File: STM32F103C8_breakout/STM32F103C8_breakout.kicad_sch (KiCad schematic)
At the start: 45 parts, among them J1 Conn1x1Pin-PA0_WKUP, J10 Conn1x1Pin-PA9, J11 Conn1x1Pin-PA10, J12 Conn1x1Pin-PA11, J13 Conn1x1Pin-PA12, J14 Conn1x1Pin-PA13, J15 Conn1x1Pin-PA14, J16 Conn1x1Pin-PA15, J17 Conn1x1Pin-PC13-TAMPER-RTC, J18 Conn1x1Pin-PC14-OSC32_IN, J19 Conn1x1Pin-PC15-OSC32_OUT, J2 Conn1x1Pin-PA1, J20 Conn1x1Pin-VBAT, J21 Conn1x1Pin-NRST, J22 BOOT0, J23 Conn1x1Pin-VDD, J24 Conn1x1Pin-VDDA, J25 Conn1x1Pin-PB15, J26 Conn1x1Pin-PB14, J27 Conn1x1Pin-PB13, J28 Conn1x1Pin-PB12, J29 Conn1x1Pin-PB11, J3 Conn1x1Pin-PA2, J30 Conn1x1Pin-PB10, J31 Conn1x1Pin-PB9, J32 Conn1x1Pin-PB8, J33 Conn1x1Pin-PB7, J34 Conn1x1Pin-PB6, J35 Conn1x1Pin-PB5, J36 Conn1x1Pin-PB4, J37 Conn1x1Pin-PB3, J38 Conn1x1Pin-PB2, J39 Conn1x1Pin-PB1, J4 Conn1x1Pin-PA3, J40 Conn1x1Pin-PB0, J41 Conn1x1Pin-PC0_OSC_IN, J42 Conn1x1Pin-PD1_OSC_OUT, J43 Conn1x1Pin-VSSA, J44 Conn1x1Pin-VSS, J5 Conn1x1Pin-PA4, J6 Conn1x1Pin-PA5, J7 Conn1x1Pin-PA6, J8 Conn1x1Pin-PA7, J9 Conn1x1Pin-PA8, U1 STM32F103C8T6

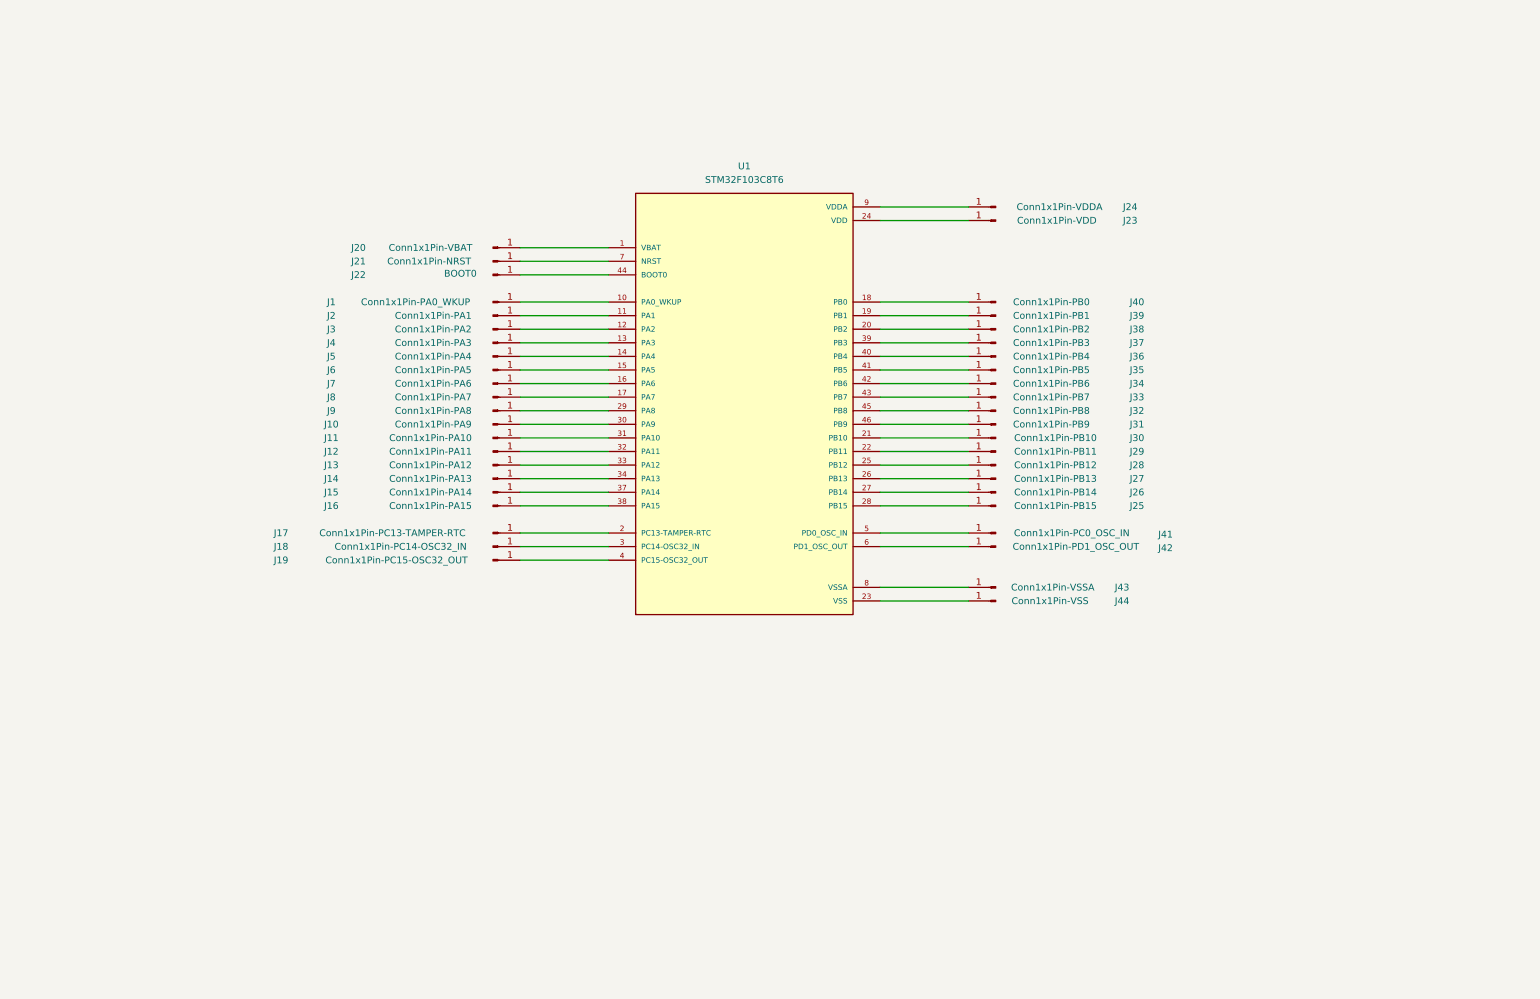
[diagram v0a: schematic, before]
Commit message: Refactored Dev. Board Schematic
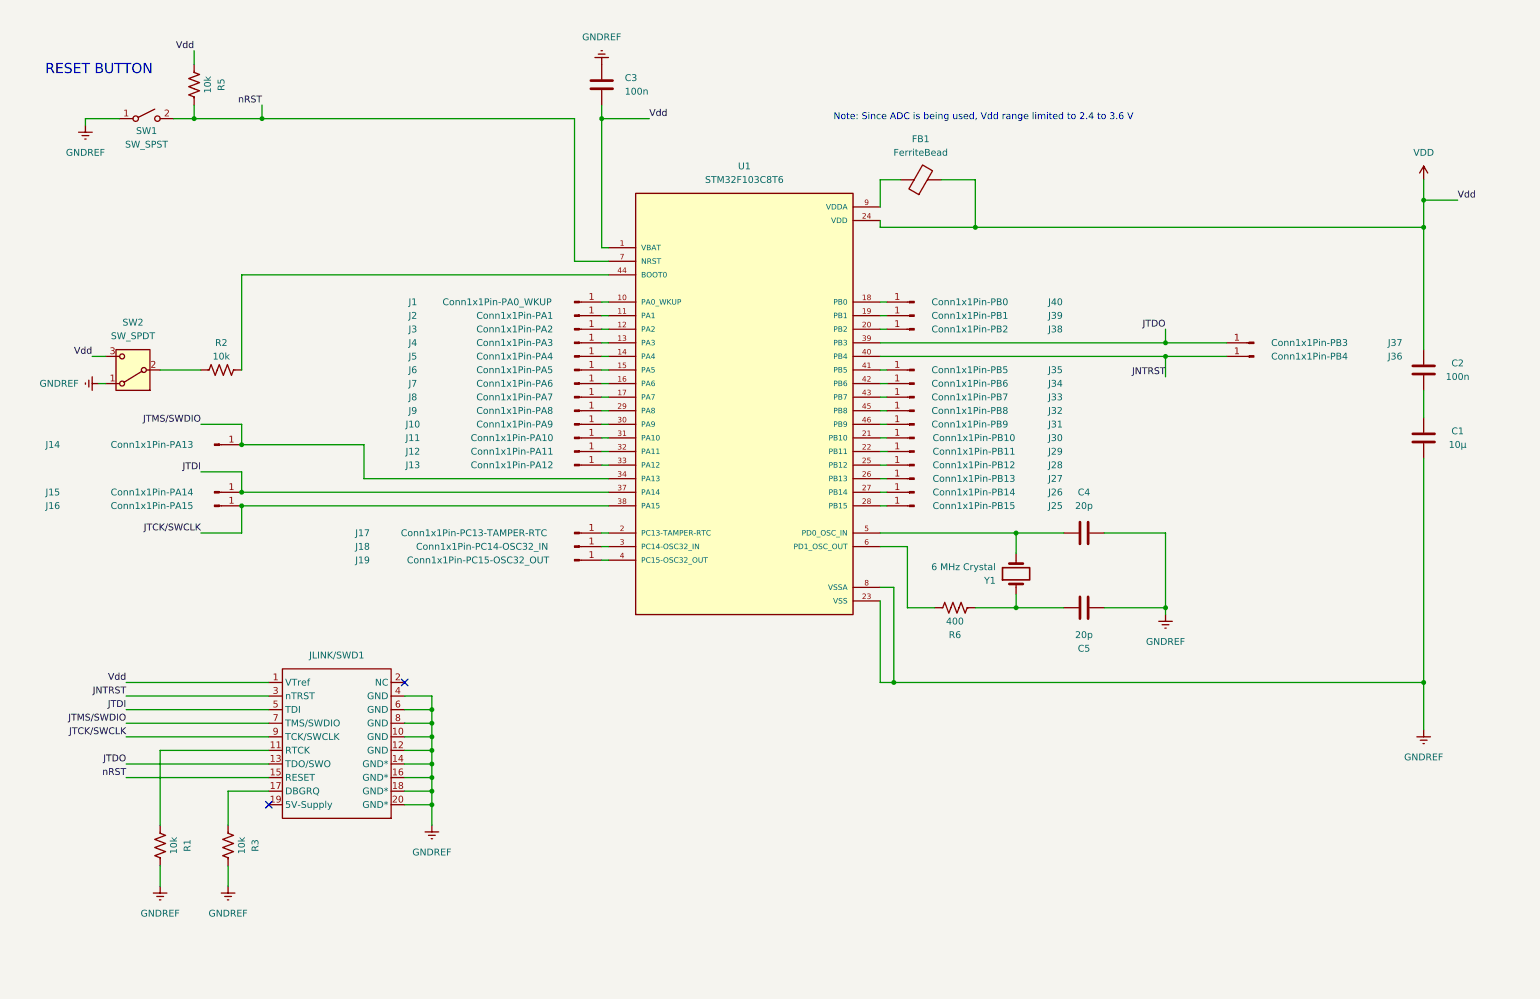
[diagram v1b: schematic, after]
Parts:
- removed J20: Conn1x1Pin-VBAT, Connector_PinHeader_2.54mm:PinHeader_1x01_P2.54mm_Horizontal, symbol Connector:Conn_01x01_Pin
- removed J21: Conn1x1Pin-NRST, Connector_PinHeader_2.54mm:PinHeader_1x01_P2.54mm_Horizontal, symbol Connector:Conn_01x01_Pin
- removed J22: BOOT0, Connector_PinHeader_2.54mm:PinHeader_1x01_P2.54mm_Horizontal, symbol Connector:Conn_01x01_Pin
- removed J23: Conn1x1Pin-VDD, Connector_PinHeader_2.54mm:PinHeader_1x01_P2.54mm_Horizontal, symbol Connector:Conn_01x01_Pin
- removed J24: Conn1x1Pin-VDDA, Connector_PinHeader_2.54mm:PinHeader_1x01_P2.54mm_Horizontal, symbol Connector:Conn_01x01_Pin
- removed J41: Conn1x1Pin-PC0_OSC_IN, Connector_PinHeader_2.54mm:PinHeader_1x01_P2.54mm_Horizontal, symbol Connector:Conn_01x01_Pin
- removed J42: Conn1x1Pin-PD1_OSC_OUT, Connector_PinHeader_2.54mm:PinHeader_1x01_P2.54mm_Horizontal, symbol Connector:Conn_01x01_Pin
- removed J43: Conn1x1Pin-VSSA, Connector_PinHeader_2.54mm:PinHeader_1x01_P2.54mm_Horizontal, symbol Connector:Conn_01x01_Pin
- removed J44: Conn1x1Pin-VSS, Connector_PinHeader_2.54mm:PinHeader_1x01_P2.54mm_Horizontal, symbol Connector:Conn_01x01_Pin
- added C1: 10μ, symbol Device:C
- added C2, C3: 100n, symbol Device:C
- added C4, C5: 20p, symbol Device:C
- added FB1: FerriteBead, symbol Device:FerriteBead
- added JLINK/SWD1: ~, symbol KnockOut_Symbols:KnockOut_Debugger
- added R1, R2, R3, R5: 10k, symbol Device:R_US
- added R6: 400, symbol Device:R_US
- added SW1: SW_SPST, symbol Switch:SW_SPST
- added SW2: SW_SPDT, symbol Switch:SW_SPDT
- added Y1: 6 MHz Crystal, symbol Device:Crystal
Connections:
- net VSS is gone; now on net GNDREF: U1.23 (VSS), U1.35 (VSS), U1.47 (VSS)
- net VDD: now also U1.1 (VBAT), C2.2, C3.1, FB1.2, JLINK/SWD1.1 (VTref), R5.1, SW2.3 (C)
- net JTDO: now reaches J37.1 (Pin_1), U1.39 (PB3)
- net JTDO: now also JLINK/SWD1.13 (TDO/SWO)
- net JTMS/SWDIO: now reaches J14.1 (Pin_1), U1.34 (PA13)
- net JTMS/SWDIO: now also JLINK/SWD1.7 (TMS/SWDIO)
- net JTDI: now reaches J15.1 (Pin_1), U1.37 (PA14)
- net JTDI: now also JLINK/SWD1.5 (TDI)
- net JTCK/SWCLK: now reaches J16.1 (Pin_1), U1.38 (PA15)
- net JTCK/SWCLK: now also JLINK/SWD1.9 (TCK/SWCLK)
- net JNTRST: now reaches J36.1 (Pin_1), U1.40 (PB4)
- net JNTRST: now also JLINK/SWD1.3 (nTRST)
- net at U1.44 (BOOT0): now also R2.2
- net at U1.5 (PD0_OSC_IN): now also C4.1, Y1.2
- net at U1.6 (PD1_OSC_OUT): now also R6.2
- net nRST: now reaches U1.7 (NRST)
- net nRST: now also JLINK/SWD1.15 (RESET), R5.2, SW1.2 (B)
- net GNDREF: now reaches U1.8 (VSSA)
- net GNDREF: now also C1.1, C3.2, C4.2, C5.1, JLINK/SWD1.10 (GND), JLINK/SWD1.12 (GND), JLINK/SWD1.14 (GND*), JLINK/SWD1.16 (GND*), JLINK/SWD1.18 (GND*), JLINK/SWD1.20 (GND*), JLINK/SWD1.4 (GND), JLINK/SWD1.6 (GND), JLINK/SWD1.8 (GND), R1.2, R3.2, SW1.1 (A), SW2.1 (A)
- net at U1.9 (VDDA): now also FB1.1
- new net: C5.2, R6.1, Y1.1
- new net: C1.2, C2.1
- new net: JLINK/SWD1.11 (RTCK), R1.1
- new net: JLINK/SWD1.17 (DBGRQ), R3.1
- new net: R2.1, SW2.2 (B)
- no-connect marks 0 -> 2
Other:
- note added: "Note: Since ADC is being used, Vdd range limited to 2.4 to 3.6 V"
- note added: "RESET BUTTON"
- moved on the sheet: J1, J10, J11, J12, J13, J14, J15, J16, J17, J18, J19, J2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

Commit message: Updated schematic to (mostly) complete Dev Board.
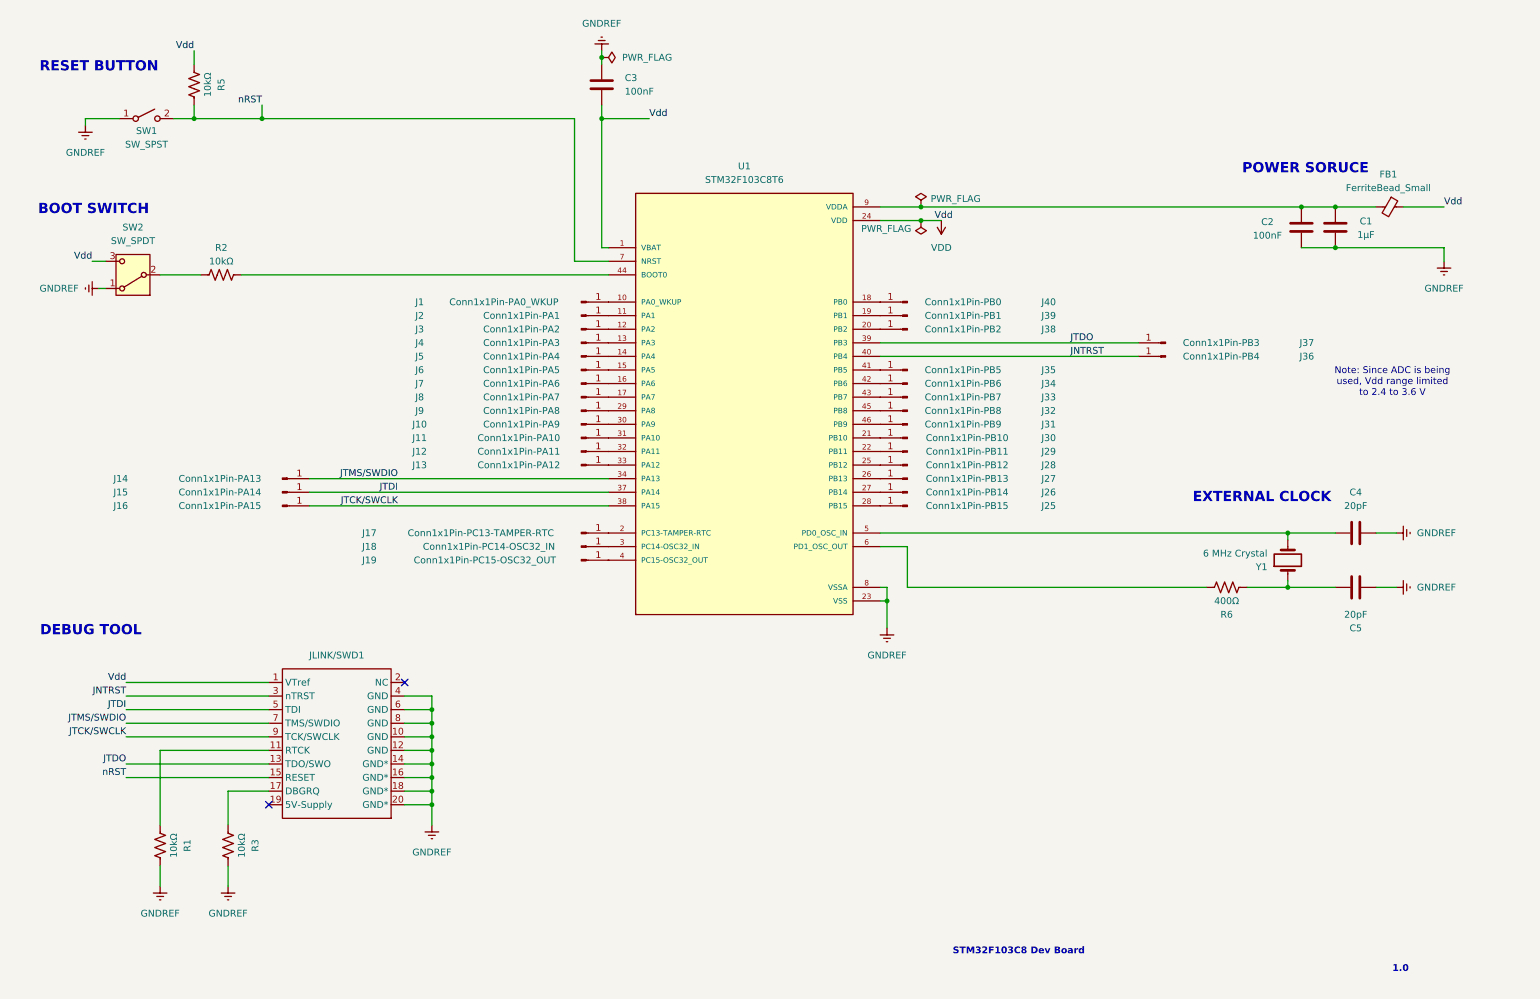
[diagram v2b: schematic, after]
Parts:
- removed FB1: FerriteBead, symbol Device:FerriteBead
- added FB1: FerriteBead_Small, Inductor_SMD:L_0805_2012Metric_Pad1.05x1.20mm_HandSolder, symbol Device:FerriteBead_Small
- C1: value 10μ -> 1μF; footprint (none) -> Capacitor_SMD:C_0805_2012Metric_Pad1.18x1.45mm_HandSolder
- C2, C3: value 100n -> 100nF; footprint (none) -> Capacitor_SMD:C_0805_2012Metric_Pad1.18x1.45mm_HandSolder
- C4, C5: value 20p -> 20pF; footprint (none) -> Capacitor_SMD:C_0805_2012Metric_Pad1.18x1.45mm_HandSolder
- JLINK/SWD1: footprint (none) -> Connector_IDC:IDC-Header_2x10_P2.54mm_Vertical
- R1, R2, R3, R5: value 10k -> 10kΩ; footprint (none) -> Resistor_SMD:R_0805_2012Metric_Pad1.20x1.40mm_HandSolder
- R6: value 400 -> 400Ω; footprint (none) -> Resistor_SMD:R_0805_2012Metric_Pad1.20x1.40mm_HandSolder
- Y1: footprint (none) -> Crystal:Crystal_SMD_HC49-SD_HandSoldering
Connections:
- net GNDREF: now also C1.2, C2.2; no longer C1.1
- net VDD: now also FB1.1; no longer C2.2
- net at U1.9 (VDDA): now also C1.1, C2.1, FB1.2
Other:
- note added: "1.0"
- note added: "BOOT SWITCH"
- note added: "DEBUG TOOL"
- note added: "EXTERNAL CLOCK"
- note added: "POWER SORUCE"
- note added: "STM32F103C8 Dev Board"
- moved on the sheet: C1, C2, C4, C5, J1, J10, J11, J12, J13, J14, J15, J16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

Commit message: Updated Boot Switch from SPDT to Jumper Functionality
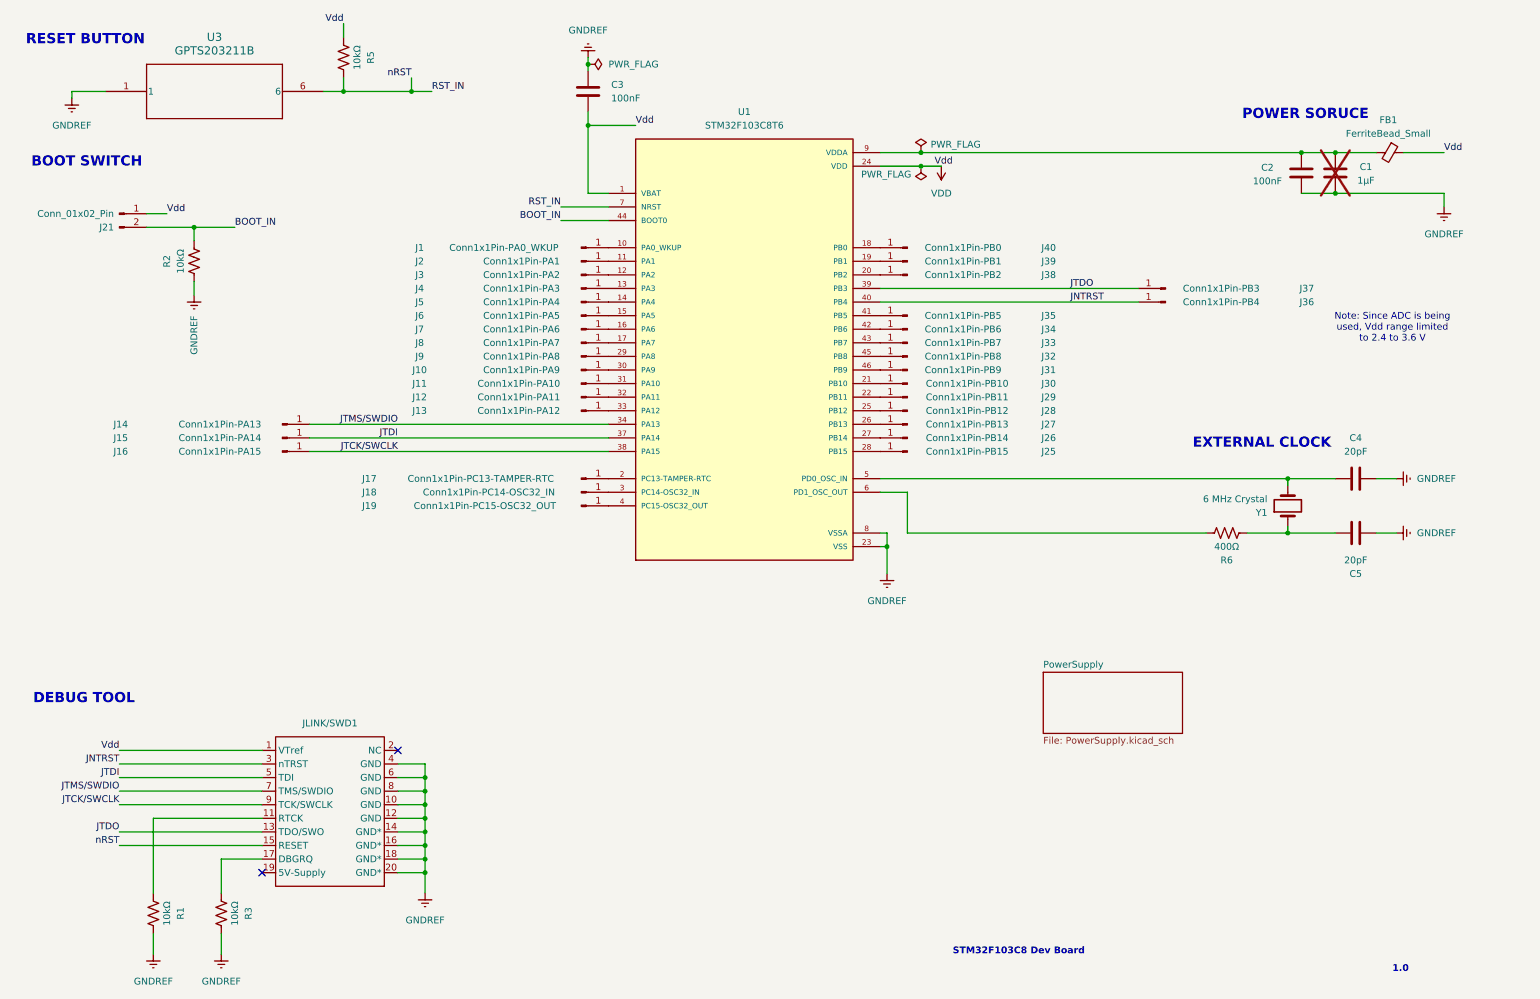
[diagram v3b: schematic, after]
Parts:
- removed SW1: SW_SPST, symbol Switch:SW_SPST
- removed SW2: SW_SPDT, symbol Switch:SW_SPDT
- added J21: Conn_01x02_Pin, Connector_PinHeader_1.00mm:PinHeader_1x02_P1.00mm_Horizontal, symbol Connector:Conn_01x02_Pin
- added U3: GPTS203211B, SWITCH_03211B, symbol SPST_BUTTON:GPTS203211B
- C1: now not fitted
- JLINK/SWD1: value ~ -> (none)
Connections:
- net GNDREF: now also R2.1, U3.1
- net VDD: now also J21.1 (Pin_1)
- net BOOT_IN: now reaches R2.2, U1.44 (BOOT0)
- net BOOT_IN: now also J21.2 (Pin_2)
- net nRST renamed RST_IN
- net RST_IN: now also U3.6
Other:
- added sheet PowerSupply (PowerSupply.kicad_sch)
- moved on the sheet: C2, C3, C4, C5, FB1, J1, J10, J11, J12, J13, J14, J15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
